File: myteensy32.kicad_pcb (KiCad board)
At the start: 2 copper layers, 35.6 x 17.8 mm, 32 parts, among them J1 Conn_01x14_Male, J2 Conn_01x14_Male, J3 USB_C_Receptacle_USB2.0, SW1 RESET, SW2 PROG, U1 MKL04Z32VLC4, U2 MK20DX256VLH7, U3 MCP2562-E-SN, U4 LT1117-3.3, Y1 32.768kHz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

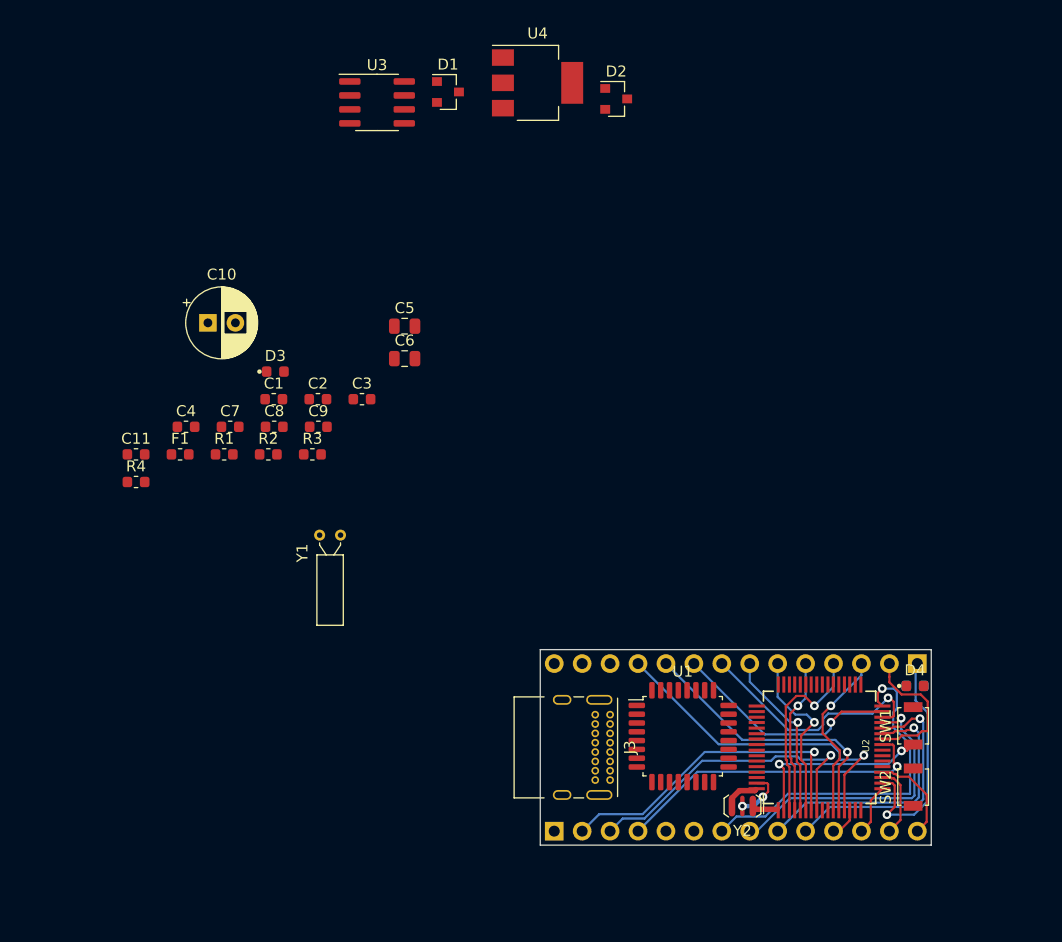
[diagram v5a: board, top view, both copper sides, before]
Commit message: rtc用の水晶は面積の問題と使わないので削除
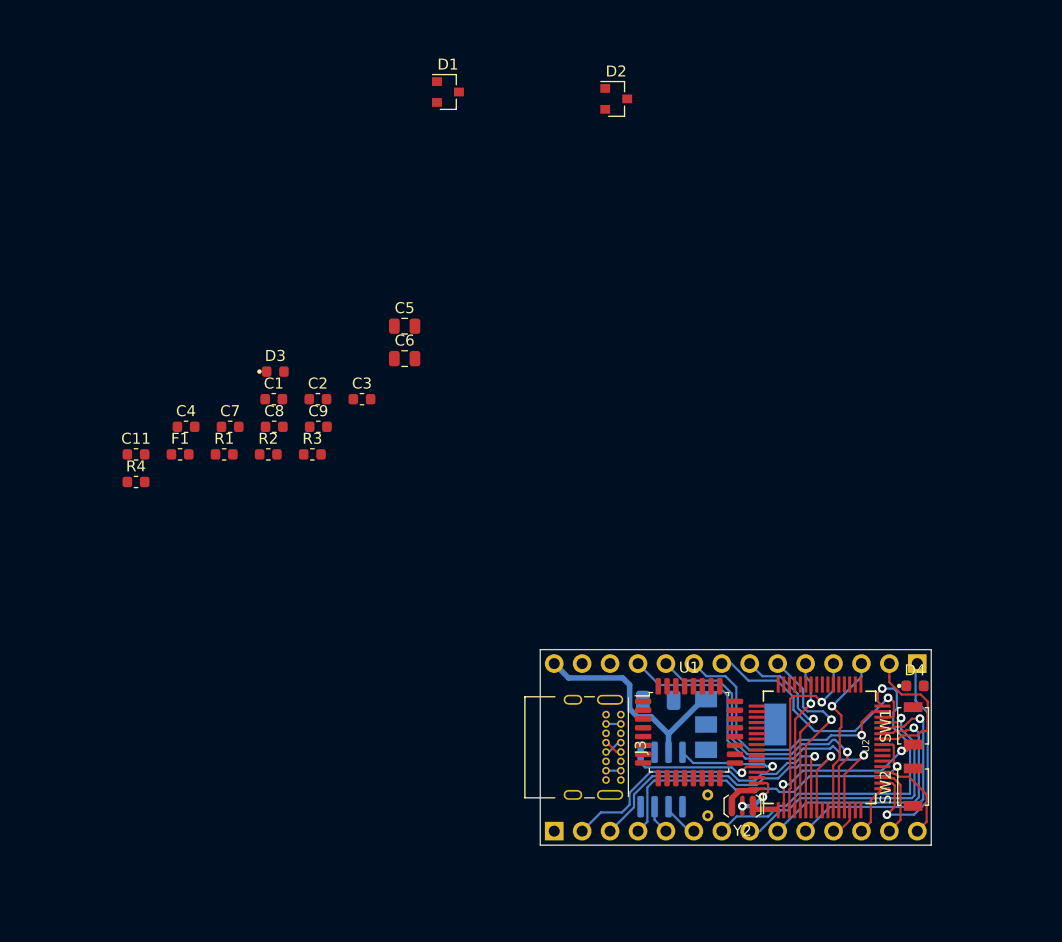
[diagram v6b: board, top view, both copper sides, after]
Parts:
- C10: footprint Capacitor_THT:CP_Radial_D6.3mm_P2.50mm -> Capacitor_SMD:C_1206_3216Metric; moved to B.Cu
- U3, U4, Y1: moved to B.Cu
- moved U3 66.8 mm to (126.6, 84.2), turned to 270 degrees
- moved U4 61.2 mm to (133.8, 79.2)
- moved C10 53.4 mm to (126.3, 77.0), turned to 180 degrees
- moved Y1 42.5 mm to (130.8, 85.6), turned to 270 degrees
- moved J3 0.98 mm to (122.9, 78.3)
- moved U1 0.68 mm to (129.1, 79.9)
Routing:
- net +5V: track 0.00 -> 20.7 mm
- net /CAN_TX: track 0.00 -> 12.2 mm, vias 0 -> 1
- net /CAN_RX: track 0.00 -> 10.4 mm, vias 0 -> 1
- net Net-(J1-Pad9): track 21.0 -> 25.2 mm
- net Net-(J1-Pad10): track 25.4 -> 28.9 mm
- net /CAN-: track 0.00 -> 3.43 mm
- net Net-(J1-Pad11): track 30.4 -> 33.7 mm
- net Net-(J2-Pad4): track 29.1 -> 31.8 mm
- net Net-(C6-Pad2): track 0.00 -> 2.70 mm
- net /CAN+: track 0.00 -> 2.65 mm
- net /USB-: track 0.00 -> 1.70 mm
- net /USB+: track 0.00 -> 1.70 mm
- net Net-(J1-Pad7): track 15.7 -> 17.4 mm
- net /RESET: track 17.3 -> 15.7 mm
- net Net-(J1-Pad6): track 16.0 -> 17.2 mm
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
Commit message: 回路図中のレギュレータを変更
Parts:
- removed Y1: 32.768kHz, Crystal:Crystal_DS26_D2.0mm_L6.0mm_Horizontal
- D2: moved to B.Cu
- moved D2 58.9 mm to (140.0, 78.5), turned to 270 degrees
- moved U1 0.32 mm to (128.8, 79.8), turned to 90 degrees
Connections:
- net +BATT renamed Net-(D2-Pad2)
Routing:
- net /PTA2: track 0.00 -> 15.1 mm
- net /PTA3: track 0.00 -> 10.7 mm
- net /RESET: track 15.7 -> 25.2 mm, vias 2 -> 3
- net /CAN_TX: track 12.2 -> 19.2 mm
- net Net-(J1-Pad5): track 14.1 -> 20.7 mm
- net Net-(J1-Pad7): track 17.4 -> 23.9 mm
- net /PTA0: track 0.00 -> 4.97 mm
- net Net-(C9-Pad1): track 0.00 -> 4.75 mm, vias 0 -> 1
- net Net-(J1-Pad6): track 17.2 -> 21.8 mm
- net /PTA1: track 0.00 -> 3.13 mm
- net +3V3: track 0.00 -> 2.79 mm
- net Net-(J1-Pad4): track 17.4 -> 19.2 mm
- net /CAN_RX: track 10.4 -> 11.8 mm
- net Net-(J2-Pad4): track 31.8 -> 33.1 mm
- net Net-(J1-Pad9): track 25.2 -> 25.7 mm
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
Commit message: 固まったのでバックアップ
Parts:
- C10: value 50uF(ESR<0.5ohm) -> 2.2u; footprint Capacitor_SMD:C_1206_3216Metric -> Capacitor_SMD:C_0805_2012Metric
- D1, R1, R2, R3: moved to B.Cu
- U4: value LT1117-3.3 -> NJM2884U1; footprint Package_TO_SOT_SMD:SOT-223-3_TabPin2 -> Package_TO_SOT_SMD:SOT-89-5
- moved C5 66.5 mm to (155.8, 83.7)
- moved D1 60.3 mm to (127.2, 78.5), turned to 270 degrees
- moved R2 56.2 mm to (142.4, 76.9), turned to 90 degrees
- moved R1 53.0 mm to (134.1, 78.5)
- moved R3 51.0 mm to (140.7, 76.9), turned to 90 degrees
- moved F1 48.2 mm to (118.5, 87.0)
- moved C6 44.5 mm to (124.5, 85.0), turned to 90 degrees
- moved U4 16.0 mm to (118.1, 82.1), turned to 90 degrees
- moved C10 9.70 mm to (116.6, 77.0), turned to 90 degrees
- moved D2 9.20 mm to (130.8, 78.5)
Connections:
- U4 pad 1: GND -> +5V
- U4 pad 2: +3V3 -> GND
- U4 pad 3: +5V -> Net-(U4-Pad3)
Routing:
- net /USB-: track 1.70 -> 37.2 mm
- net +3V3: track 2.79 -> 36.3 mm, vias 0 -> 2
- net /USB+: track 1.70 -> 33.6 mm
- net GND: track 4.65 -> 36.4 mm
- net Net-(C6-Pad2): track 2.70 -> 14.4 mm
- net Net-(J1-Pad11): track 33.7 -> 27.8 mm
- net +5V: track 20.7 -> 26.3 mm, vias 0 -> 2
- net /INTERNAL_LED: track 21.4 -> 26.9 mm
- net Net-(J1-Pad5): track 20.7 -> 15.2 mm
- net Net-(J2-Pad3): track 29.2 -> 24.3 mm
- net Net-(J1-Pad8): track 22.6 -> 17.8 mm
- net Net-(J2-Pad2): track 30.7 -> 26.2 mm
- net Net-(J1-Pad4): track 19.2 -> 23.6 mm
- net Net-(J1-Pad6): track 21.8 -> 17.5 mm
- net Net-(J1-Pad7): track 23.9 -> 19.7 mm
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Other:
- net class 0.5: via_dia 1.5 -> 0.8; via_drill 0.9 -> 0.4
